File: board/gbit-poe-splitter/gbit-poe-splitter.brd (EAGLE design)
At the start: 54.7 x 42.2 mm, 50 parts, among them IC1 LM2596HVS, U1 TPS2379DDA

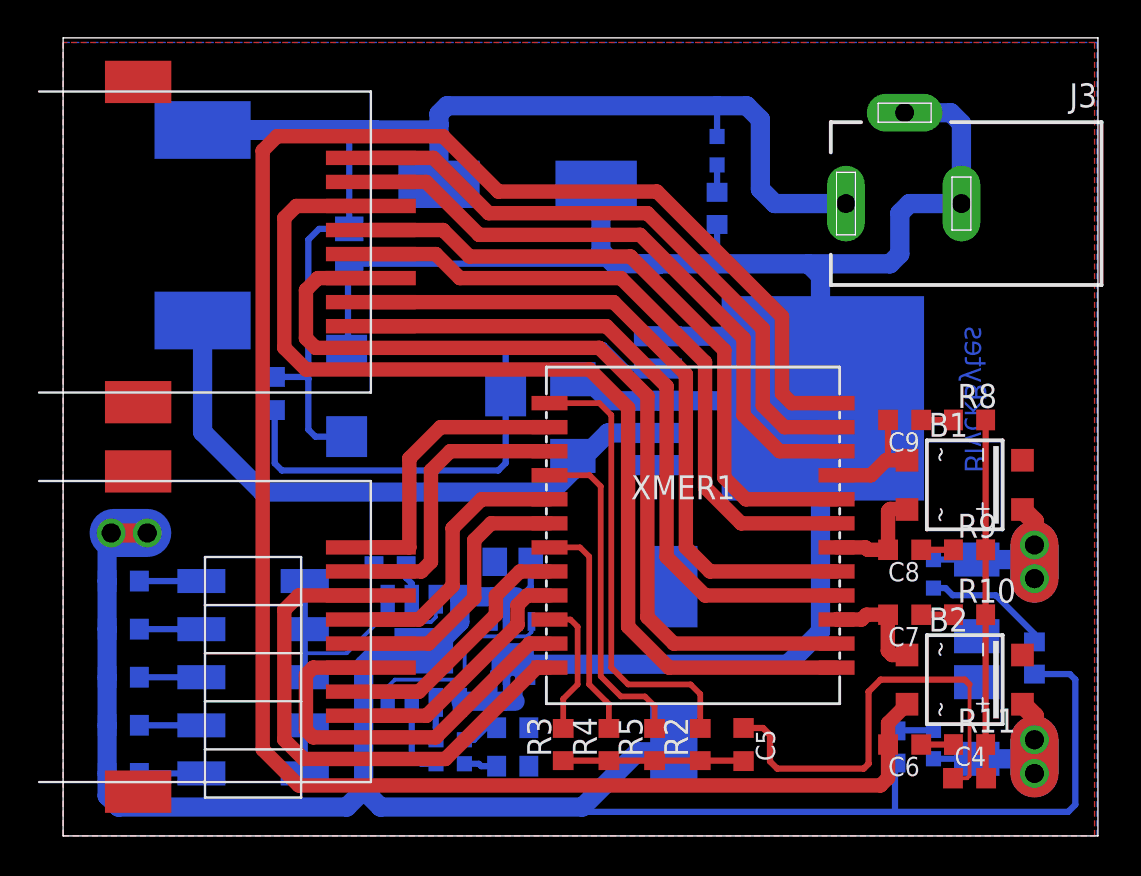
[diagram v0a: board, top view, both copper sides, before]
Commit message: Wrote first prototype summary and added partial fixes to layout
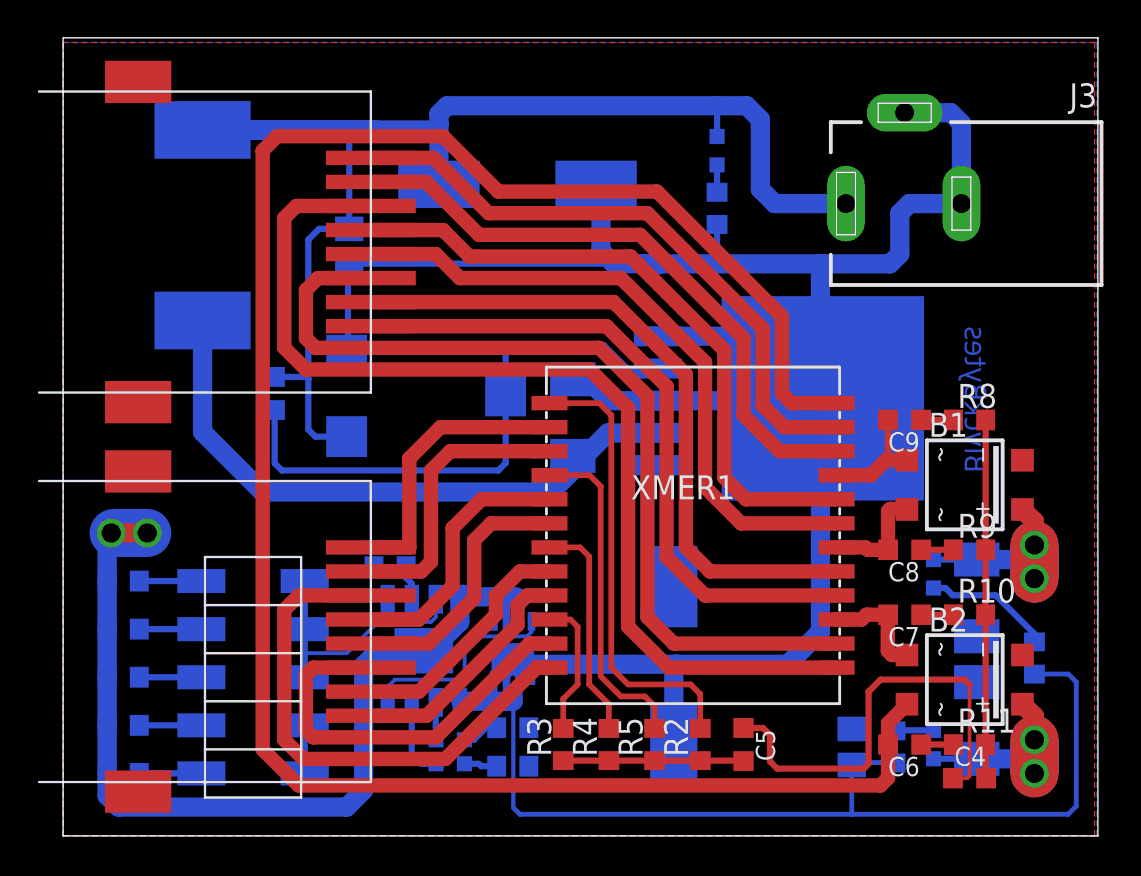
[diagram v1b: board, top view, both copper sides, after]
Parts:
- R12, R13, R14, R6, R7: value 1.91k -> 5k
- moved C10 20.4 mm to (41.7, 11.0), turned to 270 degrees
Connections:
- net GND: no longer C10.2, C12.-, R6.1, R7.1
- net RTN: now also C10.2, C12.-, R6.1, R7.1
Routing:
- net GND: track 134.8 -> 76.4 mm
- net RTN: track 127.4 -> 180.8 mm

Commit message: Fixed layout issues
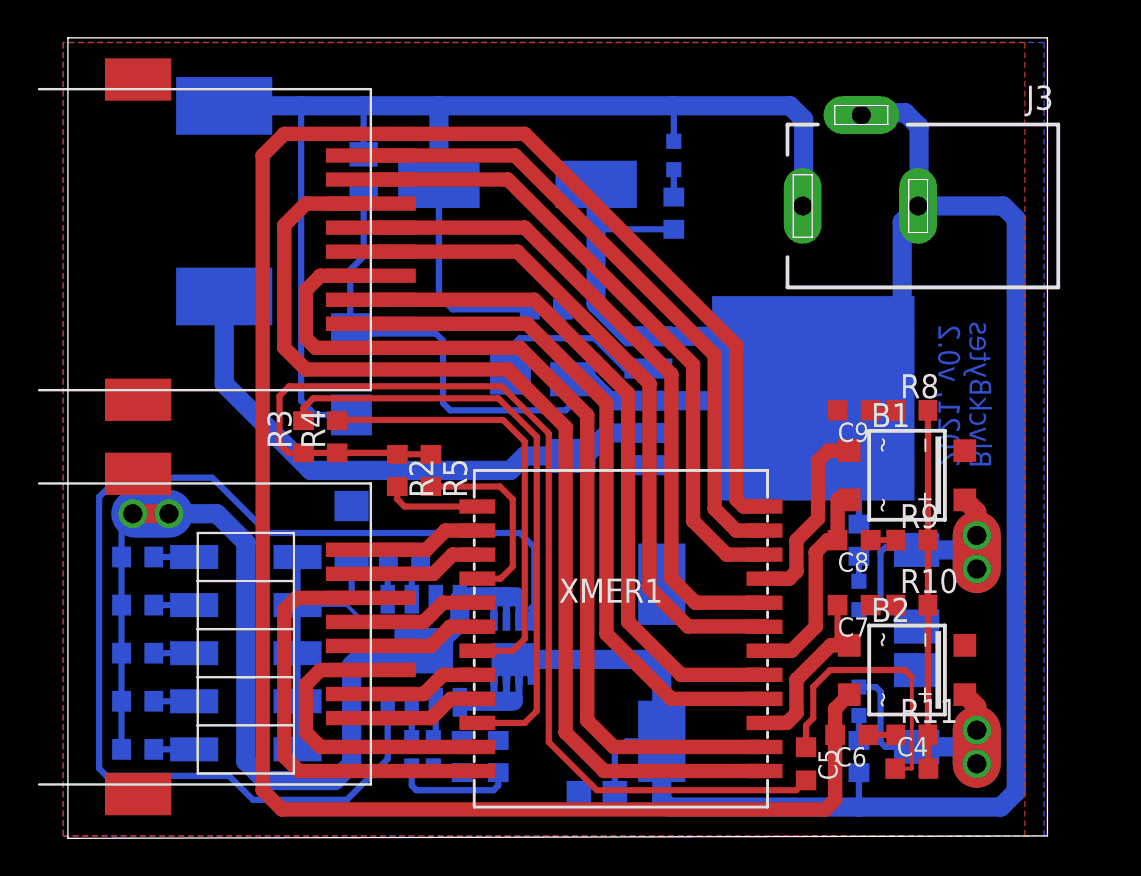
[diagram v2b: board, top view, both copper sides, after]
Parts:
- added R20: 0R, rcl:R1206
- moved R4 21.7 mm to (14.5, 27.4)
- moved R2 21.6 mm to (17.7, 25.7), turned to 270 degrees
- moved R3 21.3 mm to (12.7, 27.4)
- moved R5 18.7 mm to (19.4, 25.7), turned to 270 degrees
- moved C1 15.0 mm to (25.5, 34.2), turned to 180 degrees
- moved C10 13.7 mm to (28.2, 8.51), turned to 180 degrees
- moved R7 11.2 mm to (42.0, 22.0), turned to 270 degrees
- moved XMER1 6.66 mm to (29.5, 16.8)
- moved PSE1_ACTIVE 4.55 mm to (42.0, 13.5), turned to 180 degrees
- moved PSE2_ACTIVE 4.10 mm to (42.0, 19.1), turned to 0 degrees
- moved C11 4.01 mm to (15.9, 41.4)
- moved C5 3.45 mm to (39.2, 10.2)
- moved D1 3.24 mm to (45.1, 13.1)
- moved D2 3.22 mm to (45.1, 19.4)
- moved B1 3.09 mm to (44.6, 25.4)
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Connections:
- new net N$38: R19.1, R20.1, U1.1
- net PSE: now also R20.2; no longer R19.1, U1.1
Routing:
- net N$35: track 11.2 -> 63.1 mm
- net N$18: track 9.54 -> 57.4 mm
- net PD1B: track 7.33 -> 31.9 mm
- net PD1A: track 24.0 -> 5.06 mm
- net N$37: track 29.9 -> 11.1 mm
- net PD2A: track 11.8 -> 23.6 mm
- net RTN: track 180.8 -> 190.9 mm
- net N$2: track 14.9 -> 6.05 mm
- net N$1: track 14.8 -> 6.05 mm
- net N$4: track 13.9 -> 6.05 mm
- net N$5: track 13.9 -> 6.05 mm
- net PD2B: track 17.7 -> 10.3 mm
- net N$8: track 12.7 -> 6.05 mm
- net N$7: track 12.7 -> 6.05 mm
- net N$38: track 0.00 -> 6.04 mm
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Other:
- board size 54.7 x 42.2 mm -> 51.7 x 42.3 mm
- board text added: "2021, v0.2"

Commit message: Fixed board edge
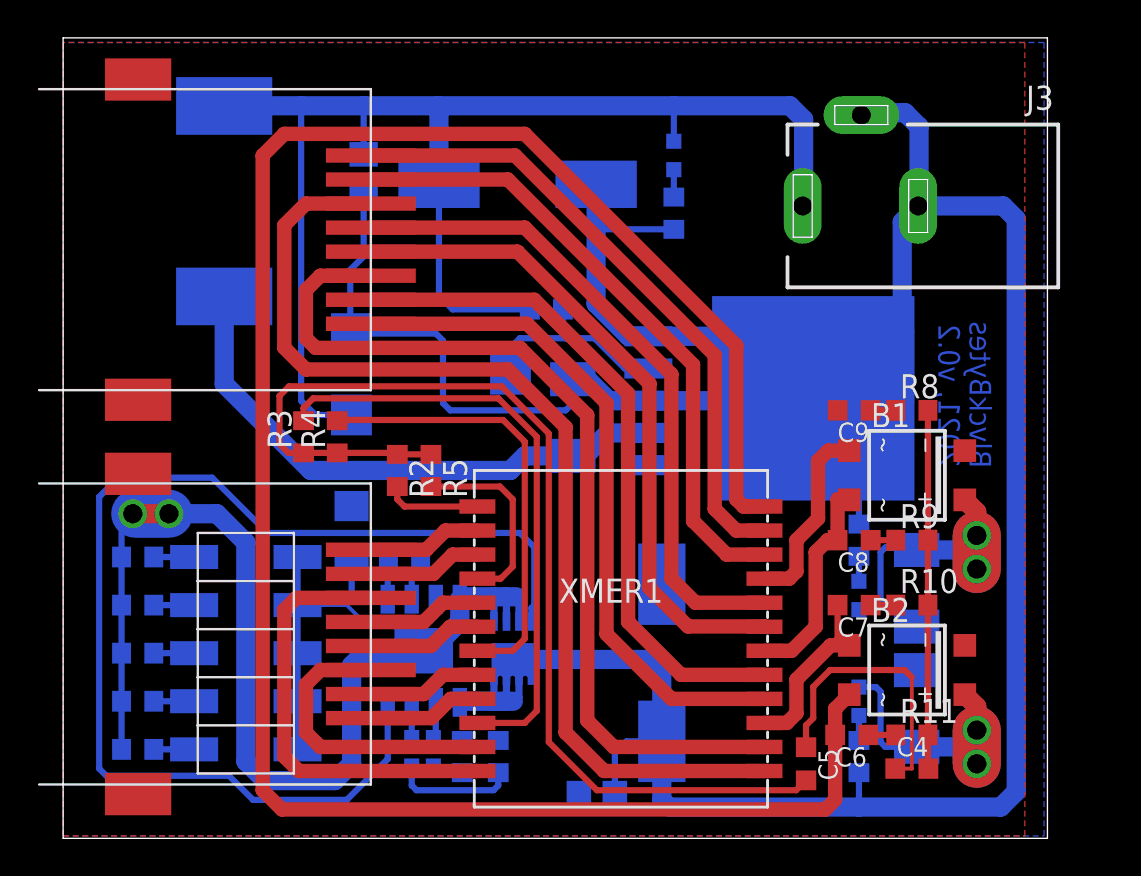
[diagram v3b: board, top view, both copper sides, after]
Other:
- board size 51.7 x 42.3 mm -> 52 x 42.3 mm
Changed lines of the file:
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@@
 <grid distance="50" unitdist="mil" unit="mil" style="lines" multiple="1" display="no" altdistance="5" altunitdist="mil" altunit="mil"/>
 <layers>
-<layer number="1" name="Top" color="4" fill="1" visible="no" active="yes"/>
+<layer number="1" name="Top" color="4" fill="1" visible="yes" active="yes"/>
 <layer number="16" name="Bottom" color="1" fill="1" visible="yes" active="yes"/>
 <layer number="17" name="Pads" color="2" fill="1" visible="yes" active="yes"/>
@@
 <layer number="19" name="Unrouted" color="6" fill="1" visible="yes" active="yes"/>
 <layer number="20" name="Dimension" color="24" fill="1" visible="yes" active="yes"/>
-<layer number="21" name="tPlace" color="7" fill="1" visible="no" active="yes"/>
+<layer number="21" name="tPlace" color="7" fill="1" visible="yes" active="yes"/>
 <layer number="22" name="bPlace" color="7" fill="1" visible="yes" active="yes"/>
-<layer number="23" name="tOrigins" color="15" fill="1" visible="no" active="yes"/>
+<layer number="23" name="tOrigins" color="15" fill="1" visible="yes" active="yes"/>
 <layer number="24" name="bOrigins" color="15" fill="1" visible="yes" active="yes"/>
-<layer number="25" name="tNames" color="7" fill="1" visible="no" active="yes"/>
+<layer number="25" name="tNames" color="7" fill="1" visible="yes" active="yes"/>
 <layer number="26" name="bNames" color="7" fill="1" visible="yes" active="yes"/>
 <layer number="27" name="tValues" color="7" fill="1" visible="no" active="yes"/>
@@
 <layer number="37" name="tTest" color="7" fill="1" visible="no" active="yes"/>
 <layer number="38" name="bTest" color="7" fill="1" visible="no" active="yes"/>
-<layer number="39" name="tKeepout" color="4" fill="11" visible="no" active="yes"/>
+<layer number="39" name="tKeepout" color="4" fill="11" visible="yes" active="yes"/>
 <layer number="40" name="bKeepout" color="1" fill="11" visible="yes" active="yes"/>
-<layer number="41" name="tRestrict" color="4" fill="10" visible="no" active="yes"/>
+<layer number="41" name="tRestrict" color="4" fill="10" visible="yes" active="yes"/>
 <layer number="42" name="bRestrict" color="1" fill="10" visible="yes" active="yes"/>
 <layer number="43" name="vRestrict" color="2" fill="10" visible="no" active="yes"/>
@@
 <layer number="49" name="Reference" color="7" fill="1" visible="no" active="yes"/>
 <layer number="50" name="dxf" color="7" fill="1" visible="no" active="no"/>
-<layer number="51" name="tDocu" color="7" fill="1" visible="no" active="yes"/>
+<layer number="51" name="tDocu" color="7" fill="1" visible="yes" active="yes"/>
 <layer number="52" name="bDocu" color="7" fill="1" visible="yes" active="yes"/>
 <layer number="53" name="tGND_GNDA" color="7" fill="9" visible="no" active="no"/>
@@
 <board>
 <plain>
-<wire x1="0.254" y1="6.223" x2="51.994" y2="6.35" width="0" layer="20"/>
-<wire x1="51.994" y1="6.35" x2="51.994" y2="48.504" width="0" layer="20"/>
-<wire x1="51.994" y1="48.504" x2="0.254" y2="48.504" width="0" layer="20"/>
-<wire x1="0.254" y1="48.504" x2="0.254" y2="6.223" width="0" layer="20"/>
+<wire x1="0" y1="6.223" x2="51.9938" y2="6.223" width="0" layer="20"/>
+<wire x1="51.9938" y1="6.223" x2="51.994" y2="48.504" width="0" layer="20"/>
+<wire x1="51.994" y1="48.504" x2="0" y2="48.504" width="0" layer="20"/>
+<wire x1="0" y1="48.504" x2="0" y2="6.223" width="0" layer="20"/>
 <text x="49.022" y="33.528" size="1.143" layer="16" font="vector" ratio="15" rot="MR270">BlvckBytes</text>
 <text x="47.371" y="33.401" size="1.143" layer="16" font="vector" ratio="15" rot="MR270">2021, v0.2</text>
@@
 </polygon>
 <contactref element="R20" pad="2"/>
-<wire x1="22.987" y1="11.391" x2="31.623" y2="19.644" width="0" layer="19" extent="16-16"/>
 </signal>
 <signal name="N$24">

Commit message: Added finished product images
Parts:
- moved U$1 0.25 mm to (24.0, 16.3)
- moved C4 0.25 mm to (45.1, 9.91)
- moved C7 0.25 mm to (41.5, 18.5)
- moved C8 0.25 mm to (41.5, 22.0)
- moved C9 0.25 mm to (41.5, 28.8)
- moved R10 0.25 mm to (45.1, 18.5)
- moved R11 0.25 mm to (45.1, 11.7)
- moved R8 0.25 mm to (45.1, 28.8)
- moved R9 0.25 mm to (45.1, 22.0)
- moved C6 0.13 mm to (41.5, 11.7)
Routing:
- net RTN: track 190.9 -> 188.9 mm
- net N$35: track 63.1 -> 64.0 mm
- net GND: track 73.9 -> 74.5 mm
- net PSE2A: track 11.4 -> 10.8 mm
- net N$23: track 1.32 -> 1.83 mm
- net N$22: track 1.32 -> 1.83 mm
- net N$21: track 1.32 -> 1.83 mm
